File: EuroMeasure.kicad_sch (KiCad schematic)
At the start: 33 parts, among them SW1 SW_DIP_x04, SW2 RST, U10 AZ1117-3V3, U11 STM32G030CxT, Y1 16MHz

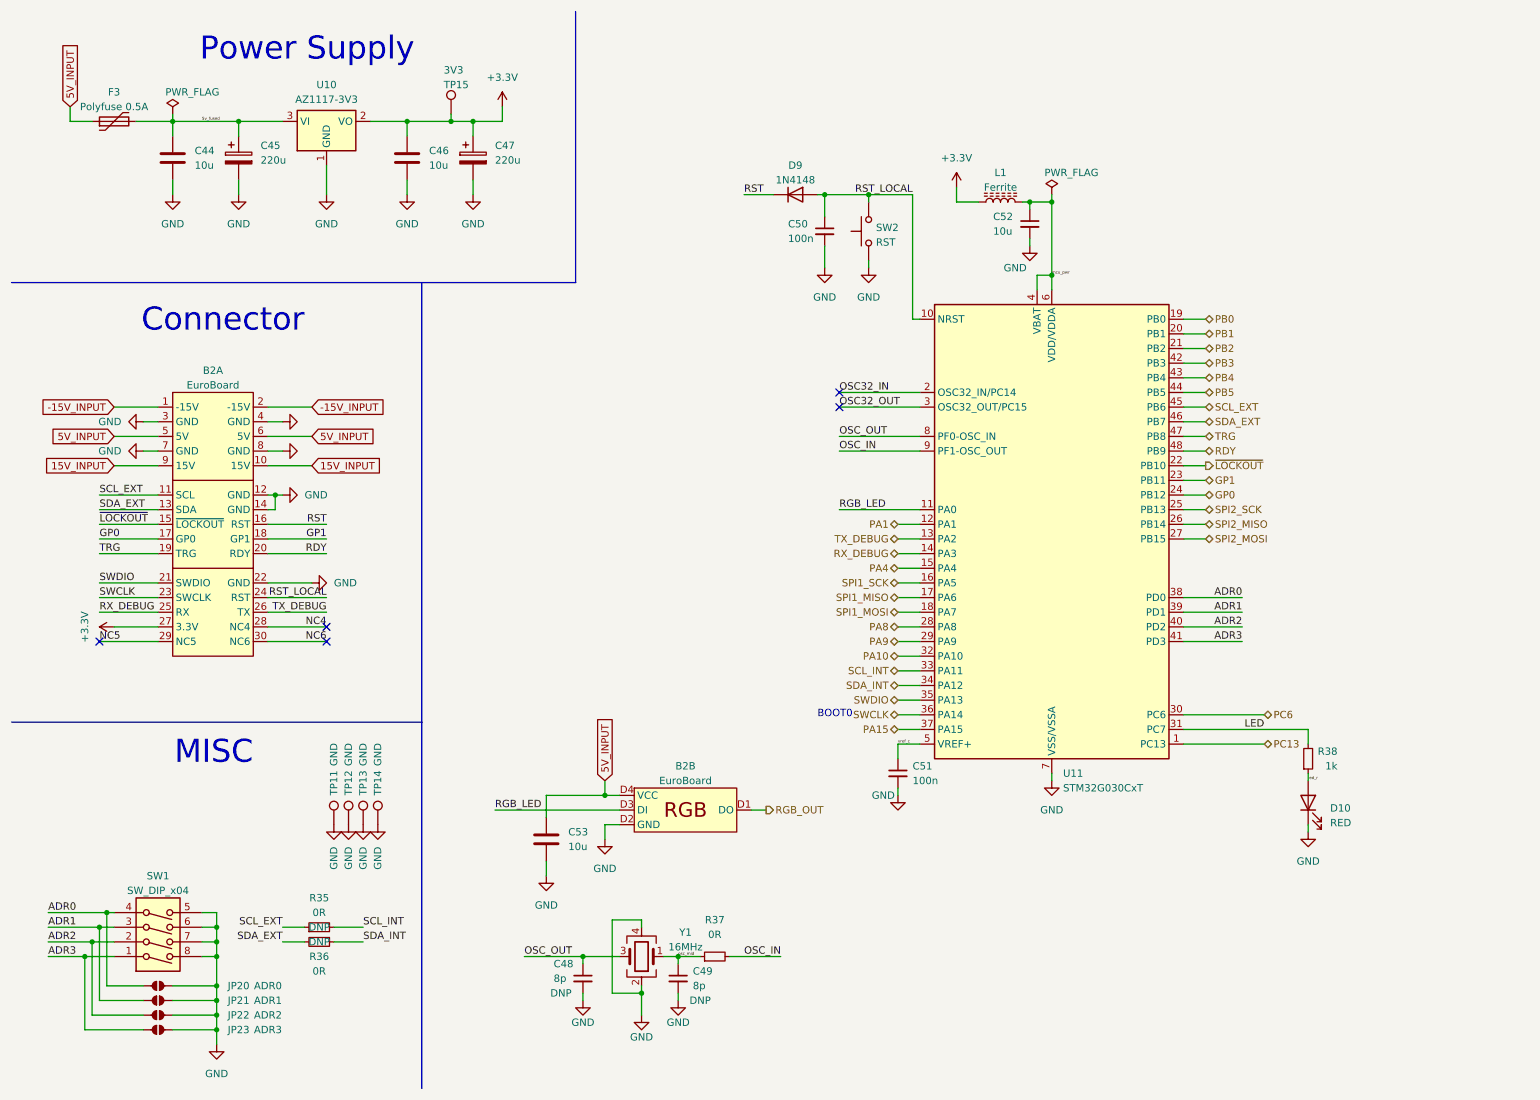
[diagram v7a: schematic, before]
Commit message: Revised sheet path
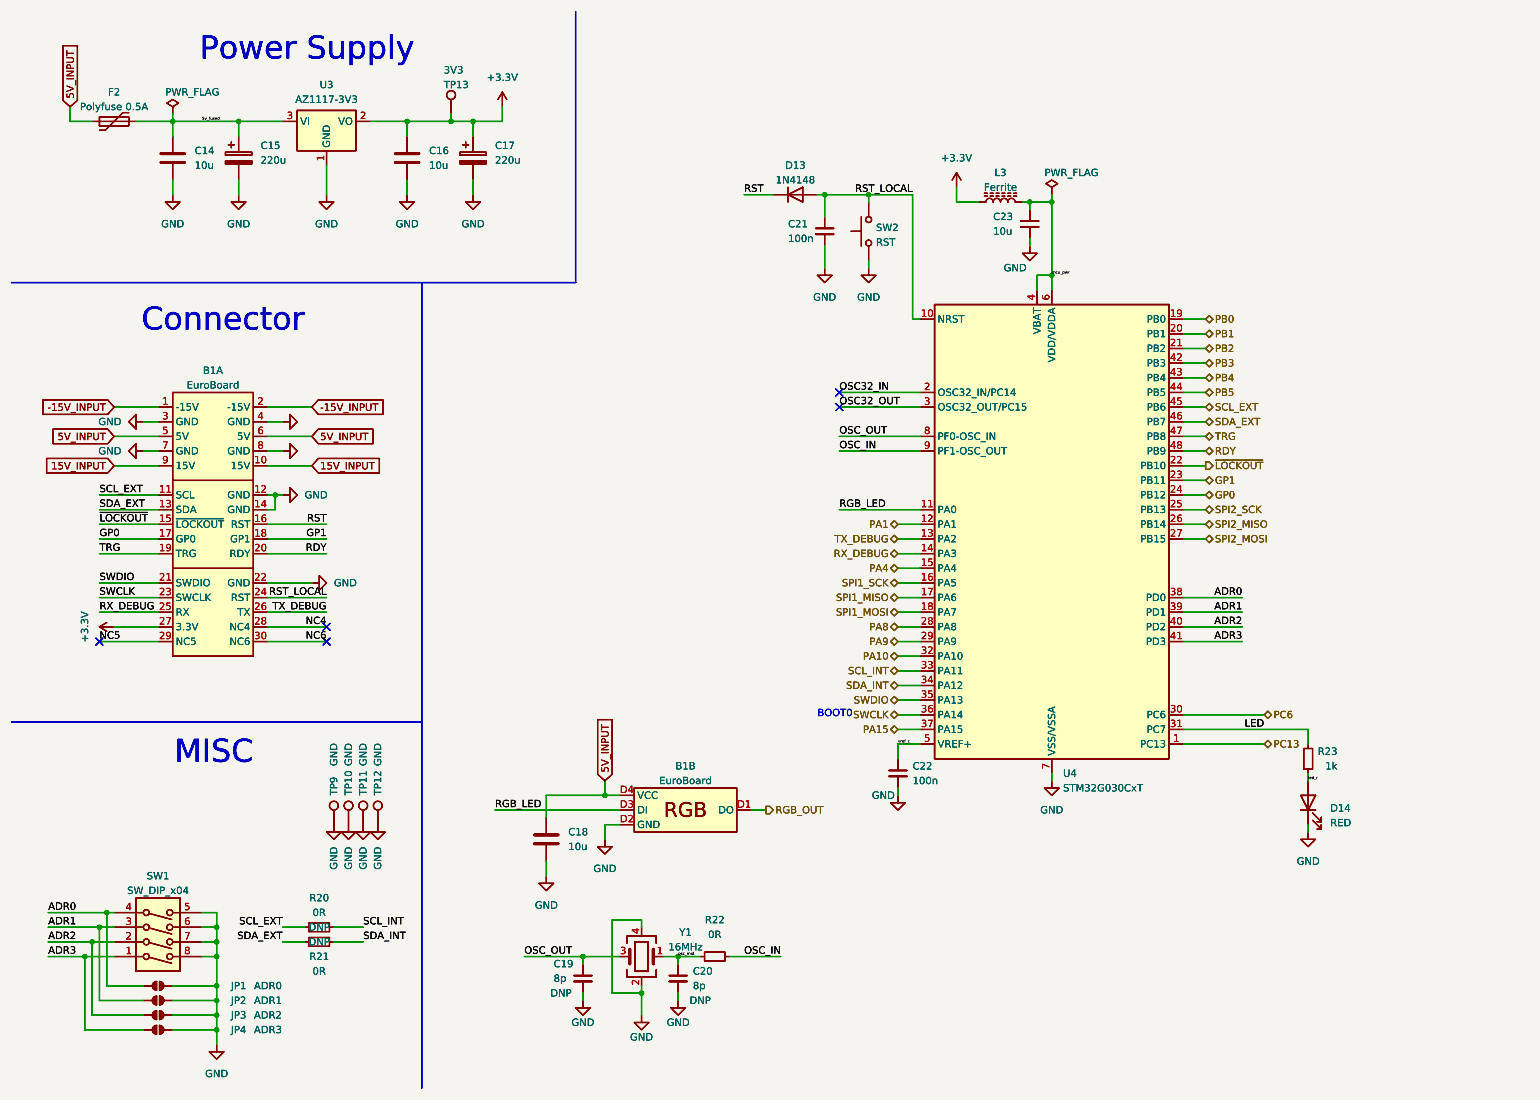
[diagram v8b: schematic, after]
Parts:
- added B1: EuroBoard, MEMS_Custom:EuroMeasureLED, symbol MEMS_Custom:EuroBoardLED
- added C14, C16, C18: 10u, Capacitor_SMD:C_0805_2012Metric_Pad1.18x1.45mm_HandSolder, symbol Device:C
- added C15, C17: 220u, Capacitor_SMD:CP_Elec_6.3x7.7, symbol Device:C_Polarized
- added C19, C20: 8p, Capacitor_SMD:C_0805_2012Metric_Pad1.18x1.45mm_HandSolder, symbol Device:C_Small
- added C21, C22: 100n, Capacitor_SMD:C_0805_2012Metric_Pad1.18x1.45mm_HandSolder, symbol Device:C_Small
- added C23: 10u, Capacitor_SMD:C_0805_2012Metric_Pad1.18x1.45mm_HandSolder, symbol Device:C_Small
- added D13: 1N4148, Diode_SMD:D_SOD-323F, symbol MEMS_Discrete-semiconductor:D_1N4148WS-SOD323
- added D14: RED, LED_SMD:LED_0805_2012Metric_Pad1.15x1.40mm_HandSolder, symbol MEMS_Discrete-semiconductor:LED_0805_Red
- added F2: Polyfuse 0.5A, Fuse:Fuse_1210_3225Metric, symbol MEMS_Protection:Polyfuse-500mA-1206L050/15YR
- added JP1: ADR0, MEMS_Passive:R_0805_2012Metric_Jumper, symbol MEMS_Passive:SolderableJumper
- added JP2: ADR1, MEMS_Passive:R_0805_2012Metric_Jumper, symbol MEMS_Passive:SolderableJumper
- added JP3: ADR2, MEMS_Passive:R_0805_2012Metric_Jumper, symbol MEMS_Passive:SolderableJumper
- added JP4: ADR3, MEMS_Passive:R_0805_2012Metric_Jumper, symbol MEMS_Passive:SolderableJumper
- added L3: Ferrite, Inductor_SMD:L_0805_2012Metric_Pad1.15x1.40mm_HandSolder, symbol MEMS_Passive:L_Ferrite_742792040
- added R20, R21, R22: 0R, Capacitor_SMD:C_0805_2012Metric_Pad1.18x1.45mm_HandSolder, symbol Device:R_Small
- added R23: 1k, Resistor_SMD:R_0805_2012Metric_Pad1.20x1.40mm_HandSolder, symbol Device:R_Small
- added SW1: SW_DIP_x04, Button_Switch_SMD:SW_DIP_SPSTx04_Slide_Omron_A6H-4101_W6.15mm_P1.27mm, symbol MEMS_Electromechanical:SW_DIP_A6H-4101
- added SW2: RST, Button_Switch_SMD:SW_SPST_B3S-1000, symbol MEMS_Electromechanical:SW_Push_Tact_B3S-1000
- added TP10, TP11, TP12, TP9: GND, MEMS_Custom:TestPoint_Pad_D1.0mm, symbol Connector:TestPoint
- added TP13: 3V3, MEMS_Custom:TestPoint_Pad_D1.0mm, symbol Connector:TestPoint
- added U3: AZ1117-3V3, Package_TO_SOT_SMD:SOT-223-3_TabPin2, symbol MEMS_IC:AZ1117IH-3.3TRG1-SOT223
- added U4: STM32G030CxT, Package_QFP:LQFP-48_7x7mm_P0.5mm, symbol MEMS_IC:STM32G030CxT
- added Y1: 16MHz, Oscillator:Oscillator_SMD_Abracon_ASDMB-4Pin_2.5x2.0mm, symbol MEMS_Passive:Crystal_16MHz_ECS-160-8-36CKM-TR3
- renumbered B2 to B1, C44 to C14, C45 to C15, C46 to C16, C47 to C17, C53 to C18, C48 to C19, C49 to C20, C50 to C21, C51 to C22, C52 to C23, D9 to D13, D10 to D14, F3 to F2, JP20 to JP1, JP21 to JP2, JP22 to JP3, JP23 to JP4, L1 to L3, R35 to R20, R36 to R21, R37 to R22, R38 to R23, TP12 to TP10, TP13 to TP11, TP14 to TP12, TP15 to TP13, TP11 to TP9, U10 to U3, U11 to U4
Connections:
- net +3.3V: now also B1.27 (3.3V), C16.1, C17.1, L3.1, TP13.1, U3.2 (VO)
- net -15V_INPUT: now also B1.1 (-15V), B1.2 (-15V)
- net 15V_INPUT: now also B1.10 (15V), B1.9 (15V)
- net 5V_INPUT: now also B1.5 (5V), B1.6 (5V), B1.D4 (VCC), C18.1, F2.1
- net 5v_fused: now also C14.1, C15.1, F2.2, U3.3 (VI)
- net ADR0: now also JP1.1, SW1.4, U4.38 (PD0)
- net ADR1: now also JP2.1, SW1.3, U4.39 (PD1)
- net ADR2: now also JP3.1, SW1.2, U4.40 (PD2)
- net ADR3: now also JP4.1, SW1.1, U4.41 (PD3)
- net GND: now also B1.12 (GND), B1.14 (GND), B1.22 (GND), B1.3 (GND), B1.4 (GND), B1.7 (GND), B1.8 (GND), B1.D2 (GND), C14.2, C15.2, C16.2, C17.2, C18.2, C19.2, C20.2, C21.2, C22.2, C23.2, D14.1 (K), JP1.2, JP2.2, JP3.2, JP4.2, SW1.5, SW1.6, SW1.7, SW1.8, SW2.1, TP10.1, TP11.1, TP12.1, TP9.1, U3.1 (GND), U4.7 (VSS/VSSA), Y1.2, Y1.4
- net GP0: now also B1.17 (GP0), U4.24 (PB12)
- net GP1: now also B1.18 (GP1), U4.23 (PB11)
- net LED: now also R23.2, U4.31 (PC7)
- net NC4: now also B1.28 (NC4)
- net NC5: now also B1.29 (NC5)
- net NC6: now also B1.30 (NC6)
- net OSC32_IN: now also U4.2 (OSC32_IN/PC14)
- net OSC32_OUT: now also U4.3 (OSC32_OUT/PC15)
- net OSC_IN: now also R22.2, U4.9 (PF1-OSC_OUT)
- net OSC_OUT: now also C19.1, U4.8 (PF0-OSC_IN), Y1.3
- net PA1: now also U4.12 (PA1)
- net PA10: now also U4.32 (PA10)
- net PA15: now also U4.37 (PA15)
- net PA4: now also U4.15 (PA4)
- net PA8: now also U4.28 (PA8)
- net PA9: now also U4.29 (PA9)
- net PB0: now also U4.19 (PB0)
- net PB1: now also U4.20 (PB1)
- net PB2: now also U4.21 (PB2)
- net PB3: now also U4.42 (PB3)
- net PB4: now also U4.43 (PB4)
- net PB5: now also U4.44 (PB5)
- net PC13: now also U4.1 (PC13)
- net PC6: now also U4.30 (PC6)
- net RDY: now also B1.20 (RDY), U4.48 (PB9)
- net RGB_LED: now also B1.D3 (DI), U4.11 (PA0)
- net RGB_OUT: now also B1.D1 (DO)
- net RST: now also B1.16 (RST), D13.1 (K)
- net RST_LOCAL: now also B1.24 (RST), C21.1, D13.2 (A), SW2.2, U4.10 (NRST)
- net RX_DEBUG: now also B1.25 (RX), U4.14 (PA3)
- net SCL_EXT: now also B1.11 (SCL), R20.1, U4.45 (PB6)
- net SCL_INT: now also R20.2, U4.33 (PA11)
- net SDA_EXT: now also B1.13 (SDA), R21.2, U4.46 (PB7)
- net SDA_INT: now also R21.1, U4.34 (PA12)
- net SPI1_MISO: now also U4.17 (PA6)
- net SPI1_MOSI: now also U4.18 (PA7)
- net SPI1_SCK: now also U4.16 (PA5)
- net SPI2_MISO: now also U4.26 (PB14)
- net SPI2_MOSI: now also U4.27 (PB15)
- net SPI2_SCK: now also U4.25 (PB13)
- net SWCLK: now also B1.23 (SWCLK), U4.36 (PA14)
- net SWDIO: now also B1.21 (SWDIO), U4.35 (PA13)
- net TRG: now also B1.19 (TRG), U4.47 (PB8)
- net TX_DEBUG: now also B1.26 (TX), U4.13 (PA2)
- net led_r: now also D14.2 (A), R23.1
- net mcu_pwr: now also C23.1, L3.2, U4.4 (VBAT), U4.6 (VDD/VDDA)
- net osc_mid: now also C20.1, R22.1, Y1.1
- net vref_c: now also C22.1, U4.5 (VREF+)
- net ~{LOCKOUT}: now also B1.15 (~{LOCKOUT}), U4.22 (PB10)
- no-connect marks 5 -> 10
